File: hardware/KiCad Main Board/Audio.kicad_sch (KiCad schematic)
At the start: 30 parts, among them J6 SPK_CONN_INT, J8 MIC_3.5MM, J9 SPK_2.5MM, U12 TLV320AIC3100, U8 SPH0645LM4H

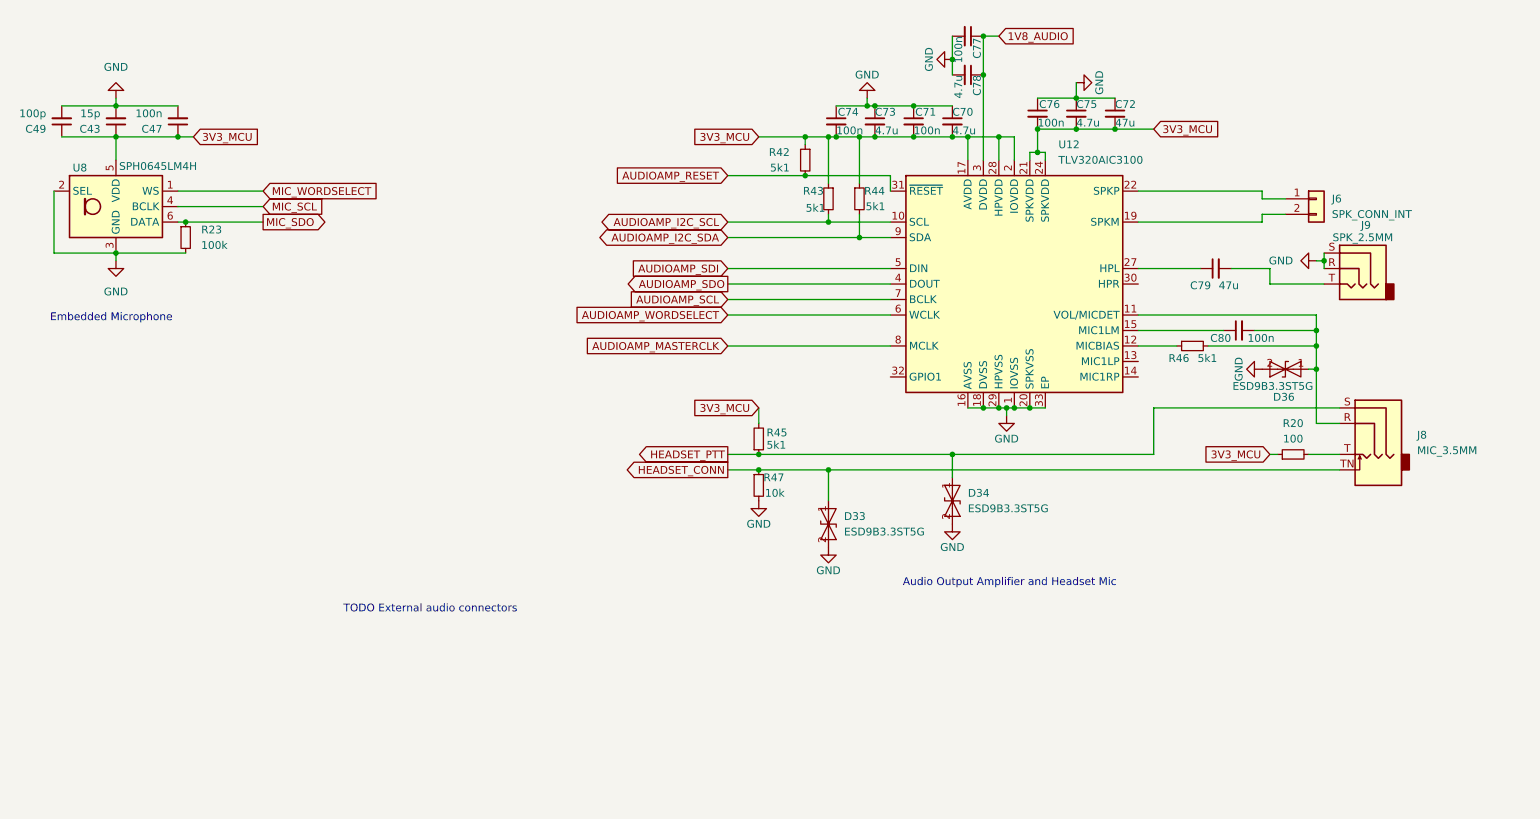
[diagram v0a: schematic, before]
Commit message: added separate project for the radio board, re-organised hardware folder
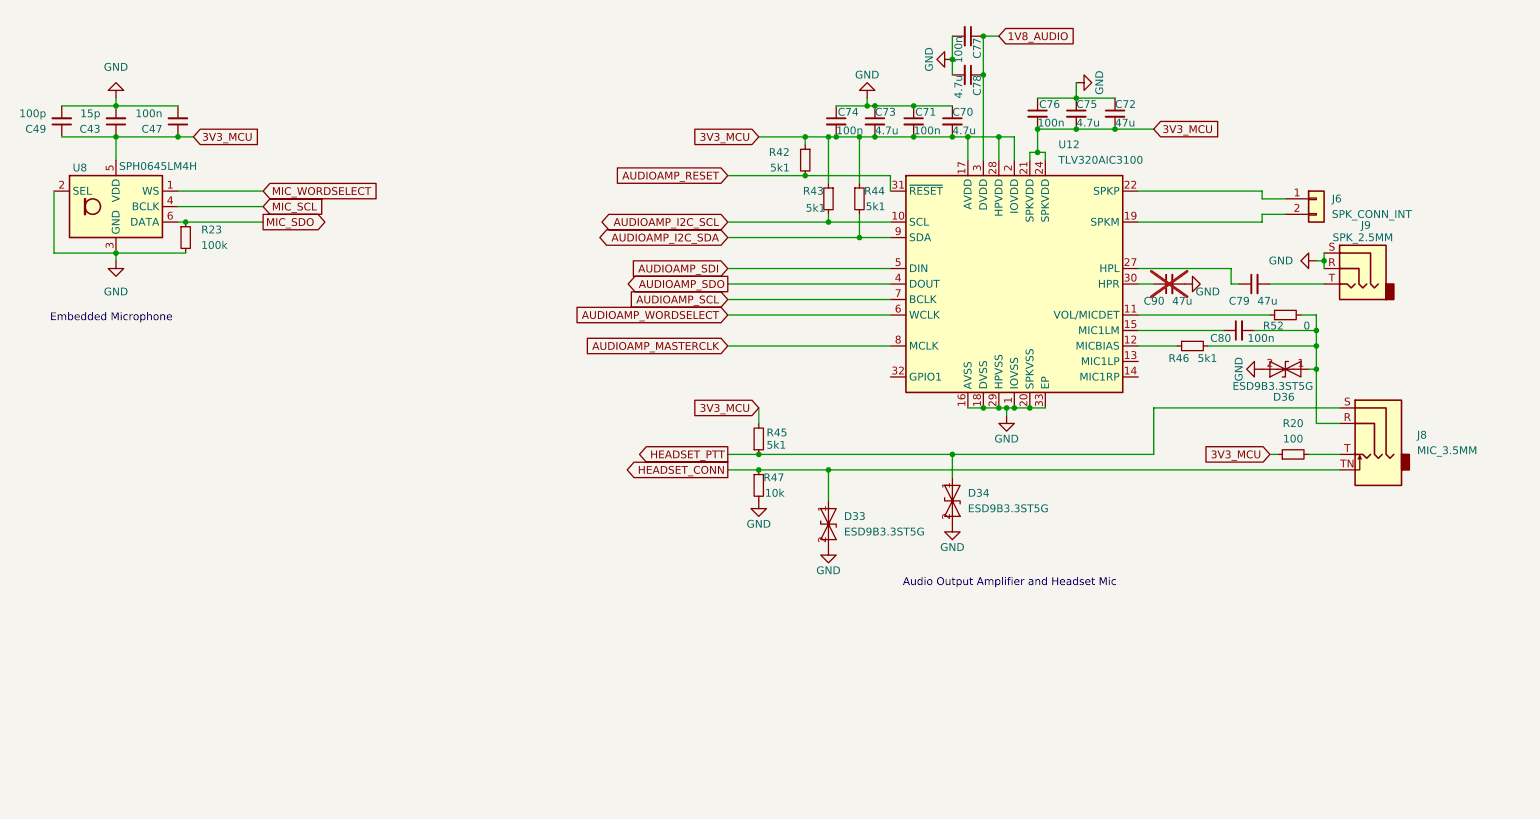
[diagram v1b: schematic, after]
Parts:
- added C90: 47u, Capacitor_SMD:C_1206_3216Metric_Pad1.33x1.80mm_HandSolder, symbol Device:C_Small
- added R52: 0, symbol Device:R_Small
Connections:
- net GND: now also C90.2
- net at C80.2, D36.1 (A1), J8.R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: now also R52.2; no longer U12.11 (VOL/MICDET)
- net at U12.30 (HPR): now also C90.1
- new net: R52.1, U12.11 (VOL/MICDET)
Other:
- note removed: "TODO External audio connectors"
- moved on the sheet: C79
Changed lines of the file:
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@@
 		)
 	)
-	(text "TODO External audio connectors\n"
-		(exclude_from_sim no)
-		(at 102.362 123.19 0)
-		(effects
-			(font
-				(size 1.27 1.27)
-			)
-		)
-	)
 	(text "Audio Output Amplifier and Headset Mic"
 		(exclude_from_sim no)
@@
 	(wire
 		(pts
-			(xy 240.03 67.31) (xy 233.68 67.31)
+			(xy 163.83 52.07) (xy 177.8 52.07)
 		)
 		(stroke
@@
 	(wire
 		(pts
-			(xy 163.83 52.07) (xy 177.8 52.07)
+			(xy 181.61 40.64) (xy 187.96 40.64)
 		)
 		(stroke
@@
 	(wire
 		(pts
-			(xy 181.61 40.64) (xy 187.96 40.64)
+			(xy 248.92 66.04) (xy 248.92 64.77)
 		)
 		(stroke
@@
 	(wire
 		(pts
-			(xy 248.92 66.04) (xy 248.92 64.77)
+			(xy 238.76 55.88) (xy 242.57 55.88)
 		)
 		(stroke
@@
 	(wire
 		(pts
-			(xy 238.76 55.88) (xy 242.57 55.88)
+			(xy 238.76 58.42) (xy 238.76 59.69)
 		)
 		(stroke
@@
 	(wire
 		(pts
-			(xy 238.76 58.42) (xy 238.76 59.69)
+			(xy 233.68 67.31) (xy 218.44 67.31)
 		)
 		(stroke
@@
 	(wire
 		(pts
-			(xy 228.6 67.31) (xy 218.44 67.31)
+			(xy 234.95 69.85) (xy 233.68 69.85)
 		)
 		(stroke
@@
 	(wire
 		(pts
-			(xy 218.44 74.93) (xy 247.65 74.93)
+			(xy 218.44 74.93) (xy 240.03 74.93)
 		)
 		(stroke
@@
 	(wire
 		(pts
+			(xy 218.44 69.85) (xy 220.98 69.85)
+		)
+		(stroke
+			(width 0)
+			(type default)
+		)
+	)
+	(wire
+		(pts
 			(xy 200.66 49.53) (xy 200.66 48.26)
 		)
@@
 	(wire
 		(pts
-			(xy 240.03 69.85) (xy 240.03 67.31)
+			(xy 195.58 29.21) (xy 193.04 29.21)
 		)
 		(stroke
@@
 	(wire
 		(pts
-			(xy 195.58 29.21) (xy 193.04 29.21)
+			(xy 181.61 45.72) (xy 175.26 45.72)
 		)
 		(stroke
@@
 	(wire
 		(pts
-			(xy 181.61 45.72) (xy 175.26 45.72)
+			(xy 74.93 54.61) (xy 60.96 54.61)
 		)
 		(stroke
@@
 	(wire
 		(pts
-			(xy 74.93 54.61) (xy 60.96 54.61)
+			(xy 201.93 44.45) (xy 201.93 48.26)
 		)
 		(stroke
@@
 	(wire
 		(pts
-			(xy 201.93 44.45) (xy 201.93 48.26)
+			(xy 156.21 97.79) (xy 187.96 97.79)
 		)
 		(stroke
@@
 	(wire
 		(pts
-			(xy 156.21 97.79) (xy 187.96 97.79)
+			(xy 50.8 39.37) (xy 50.8 40.64)
 		)
 		(stroke
@@
 	(wire
 		(pts
-			(xy 50.8 39.37) (xy 50.8 40.64)
+			(xy 163.83 45.72) (xy 167.64 45.72)
 		)
 		(stroke
@@
 	(wire
 		(pts
-			(xy 163.83 45.72) (xy 167.64 45.72)
+			(xy 240.03 69.85) (xy 248.92 69.85)
 		)
 		(stroke
@@
 	(wire
 		(pts
+			(xy 233.68 69.85) (xy 233.68 67.31)
+		)
+		(stroke
+			(width 0)
+			(type default)
+		)
+	)
+	(wire
+		(pts
 			(xy 187.96 45.72) (xy 190.5 45.72)
 		)
@@
 	(wire
 		(pts
-			(xy 190.5 90.17) (xy 193.04 90.17)
+			(xy 245.11 74.93) (xy 247.65 74.93)
 		)
 		(stroke
@@
 	(wire
 		(pts
-			(xy 173.99 39.37) (xy 173.99 40.64)
+			(xy 190.5 90.17) (xy 193.04 90.17)
 		)
 		(stroke
@@
 	(wire
 		(pts
-			(xy 240.03 69.85) (xy 248.92 69.85)
+			(xy 173.99 39.37) (xy 173.99 40.64)
 		)
 		(stroke
@@
 	)
 	(symbol
+		(lib_id "Device:R_Small")
+		(at 242.57 74.93 90)
+		(mirror x)
+		(unit 1)
+		(exclude_from_sim no)
+		(in_bom yes)
+		(on_board yes)
+		(dnp no)
+		(property "Reference" "R52"
+			(at 242.316 76.708 90)
+			(effects
+				(font
+					(size 1.27 1.27)
+				)
+				(justify left)
+			)
+		)
+		(property "Value" "0"
+			(at 246.634 76.708 90)
+			(effects
+				(font
+					(size 1.27 1.27)
+				)
+				(justify left)
+			)
+		)
+		(property "Footprint" ""
+			(at 242.57 74.93 0)
+			(effects
+				(font
+					(size 1.27 1.27)
+				)
+				(hide yes)
+			)
+		)
+		(property "Datasheet" "~"
+			(at 242.57 74.93 0)
+			(effects
+				(font
+					(size 1.27 1.27)
+				)
+				(hide yes)
+			)
+		)
+		(property "Description" "Resistor, small symbol"
+			(at 242.57 74.93 0)
+			(effects
+				(font
+					(size 1.27 1.27)
+				)
+				(hide yes)
+			)
+		)
+		(pin "2"
+		)
+		(pin "1"
+		)
+		(instances
+			(project "OSS Radio Hardware Design"
+				(path "/fd5c68a7-f5d0-4135-a258-bde3ebf63307/1fea53e1-bad3-4fc0-9492-4b8e0f78b13e"
+					(reference "R52")
+					(unit 1)
+				)
+			)
+		)
+	)
+	(symbol
 		(lib_id "Device:C_Small")
 		(at 168.91 43.18 0)
@@
 	(symbol
 		(lib_id "Device:C_Small")
-		(at 231.14 67.31 90)
+		(at 237.49 69.85 90)
 		(unit 1)
 		(exclude_from_sim no)
@@
 		(dnp no)
 		(property "Reference" "C79"
-			(at 230.378 70.104 90)
+			(at 236.728 72.644 90)
 			(effects
 				(font
@@
 		)
 		(property "Value" "47u"
-			(at 234.95 70.104 90)
+			(at 241.3 72.644 90)
 			(effects
 				(font
@@
 		)
 		(property "Footprint" "Capacitor_SMD:C_1206_3216Metric_Pad1.33x1.80mm_HandSolder"
-			(at 231.14 67.31 0)
+			(at 237.49 69.85 0)
 			(effects
 				(font
@@
 		)
 		(property "Datasheet" "~"
-			(at 231.14 67.31 0)
+			(at 237.49 69.85 0)
 			(effects
 				(font
@@
 		)
 		(property "Description" "Unpolarized capacitor, small symbol"
-			(at 231.14 67.31 0)
+			(at 237.49 69.85 0)
 			(effects
 				(font
@@
 	(symbol
 		(lib_id "power:GND")
+		(at 226.06 69.85 90)
+		(unit 1)
+		(exclude_from_sim no)
+		(in_bom yes)
+		(on_board yes)
+		(dnp no)
+		(property "Reference" "#PWR068"
+			(at 232.41 69.85 0)
+			(effects
+				(font
+					(size 1.27 1.27)
+				)
+				(hide yes)
+			)
+		)
+		(property "Value" "GND"
+			(at 227.838 71.12 90)
+			(effects
+				(font
+					(size 1.27 1.27)
+				)
+				(justify right)
+			)
+		)
+		(property "Footprint" ""
+			(at 226.06 69.85 0)
+			(effects
+				(font
+					(size 1.27 1.27)
+				)
+				(hide yes)
+			)
+		)
+		(property "Datasheet" ""
+			(at 226.06 69.85 0)
+			(effects
+				(font
+					(size 1.27 1.27)
+				)
+				(hide yes)
+			)
+		)
+		(property "Description" "Power symbol creates a global label with name \"GND\" , ground"
+			(at 226.06 69.85 0)
+			(effects
+				(font
+					(size 1.27 1.27)
+				)
+				(hide yes)
+			)
+		)
+		(pin "1"
+		)
+		(instances
+			(project "OSS Radio Hardware Design"
+				(path "/fd5c68a7-f5d0-4135-a258-bde3ebf63307/1fea53e1-bad3-4fc0-9492-4b8e0f78b13e"
+					(reference "#PWR068")
+					(unit 1)
+				)
+			)
+		)
+	)
+	(symbol
+		(lib_id "power:GND")
 		(at 238.76 83.82 270)
 		(unit 1)
@@
 					(unit 1)
 				)
+			)
+		)
+	)
+	(symbol
+		(lib_id "Device:C_Small")
+		(at 223.52 69.85 90)
+		(unit 1)
+		(exclude_from_sim no)
+		(in_bom yes)
+		(on_board yes)
+		(dnp yes)
+		(property "Reference" "C90"
+			(at 222.758 72.644 90)
+			(effects
+				(font
+					(size 1.27 1.27)
+				)
+				(justify left)
+			)
+		)
+		(property "Value" "47u"
+			(at 227.33 72.644 90)
+			(effects
+				(font
+					(size 1.27 1.27)
+				)
+				(justify left)
+			)
+		)
+		(property "Footprint" "Capacitor_SMD:C_1206_3216Metric_Pad1.33x1.80mm_HandSolder"
+			(at 223.52 69.85 0)
+			(effects
+				(font
+					(size 1.27 1.27)
+				)
+				(hide yes)
+			)
+		)
+		(property "Datasheet" "~"
+			(at 223.52 69.85 0)
+			(effects
+				(font
+					(size 1.27 1.27)
+				)
+				(hide yes)
+			)
+		)
+		(property "Description" "Unpolarized capacitor, small symbol"
+			(at 223.52 69.85 0)
+			(effects
+				(font
+					(size 1.27 1.27)
+				)
+				(hide yes)
+			)
+		)
+		(pin "2"
+		)
+		(pin "1"
+		)
+		(instances
+			(project "OSS Radio Hardware Design"
+				(path "/fd5c68a7-f5d0-4135-a258-bde3ebf63307/1fea53e1-bad3-4fc0-9492-4b8e0f78b13e"
+					(reference "C90")
+					(unit 1)
+				)

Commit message: working on PCB
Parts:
- removed C78: 4.7u, Capacitor_SMD:C_0603_1608Metric_Pad1.08x0.95mm_HandSolder, symbol Device:C_Small
- removed J9: SPK_2.5MM, symbol Connector_Audio:AudioJack3
- added J7: SPK_2.5MM SJ1-2503A, SJ1-2503A:SAMESKY_SJ1-2503A, symbol SJ1-2503A:SJ1-2503A
- J6: footprint (none) -> Connector_JST:JST_PH_S2B-PH-K_1x02_P2.00mm_Horizontal
- J8: value MIC_3.5MM -> MIC_3.5MM PJ-307C; footprint (none) -> Connector_Audio:Jack_3.5mm_CUI_SJ1-3525N_Horizontal
- R20, R23, R42, R43, R44, R45, R46, R47, R52: footprint (none) -> Resistor_SMD:R_0603_1608Metric_Pad0.98x0.95mm_HandSolder
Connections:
- net GND: now also J7.1, J7.4
- net at C79.2: now also J7.2, J7.3
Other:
- moved on the sheet: C79, J6

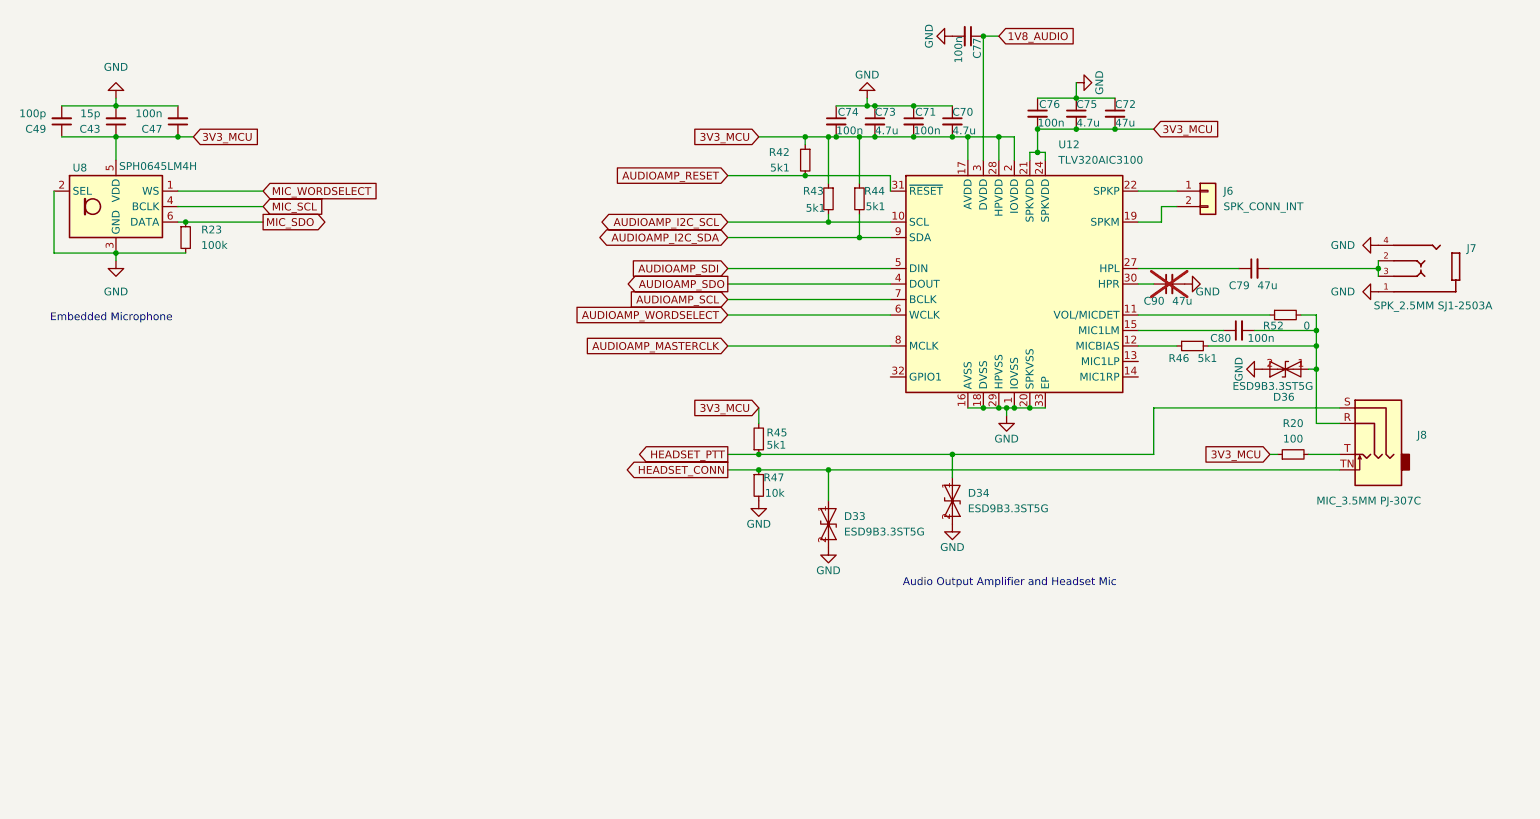
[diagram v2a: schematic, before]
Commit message: all GPIO nets connected on schematic
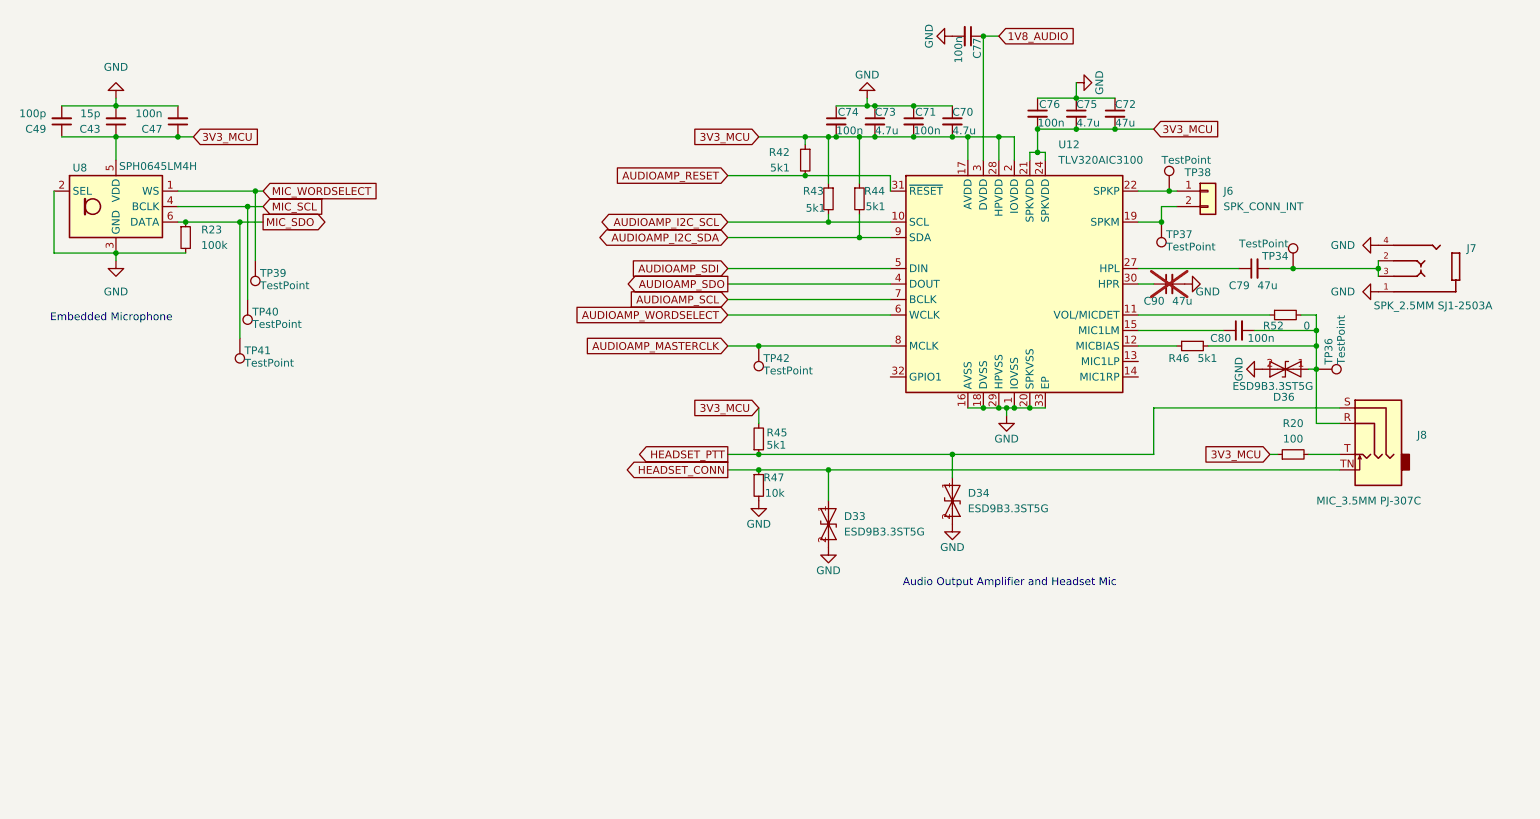
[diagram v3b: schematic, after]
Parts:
- added TP34, TP36, TP37, TP38, TP39, TP40, TP41, TP42: TestPoint, TestPoint:TestPoint_Pad_D1.0mm, symbol Connector:TestPoint
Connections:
- net AUDIOAMP_MASTERCLK: now also TP42.1
- net MIC_SCL: now also TP40.1
- net MIC_SDO: now also TP41.1
- net MIC_WORDSELECT: now also TP39.1
- net at C80.2, D36.1 (A1), J8.R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: now also TP36.1
- net at J6.2 (Pin_2), U12.19 (SPKM), U12.23 (SPKM): now also TP37.1
- net at J6.1 (Pin_1), U12.22 (SPKP), U12.26 (SPKP): now also TP38.1
- net at C79.2, J7.2, J7.3: now also TP34.1

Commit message: mostly designed PCB
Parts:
- removed TP34, TP36, TP37, TP38: TestPoint, TestPoint:TestPoint_Pad_D1.0mm, symbol Connector:TestPoint
